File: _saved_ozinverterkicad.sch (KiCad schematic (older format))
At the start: 83 parts, among them P1 CONN_02X05, P2 status, P3 on/off, P4 temp, P5 ct sense, P6 Active mains, P7 neutral mains, P8 systemled, Q2 tip35c, T1 12vac transforme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

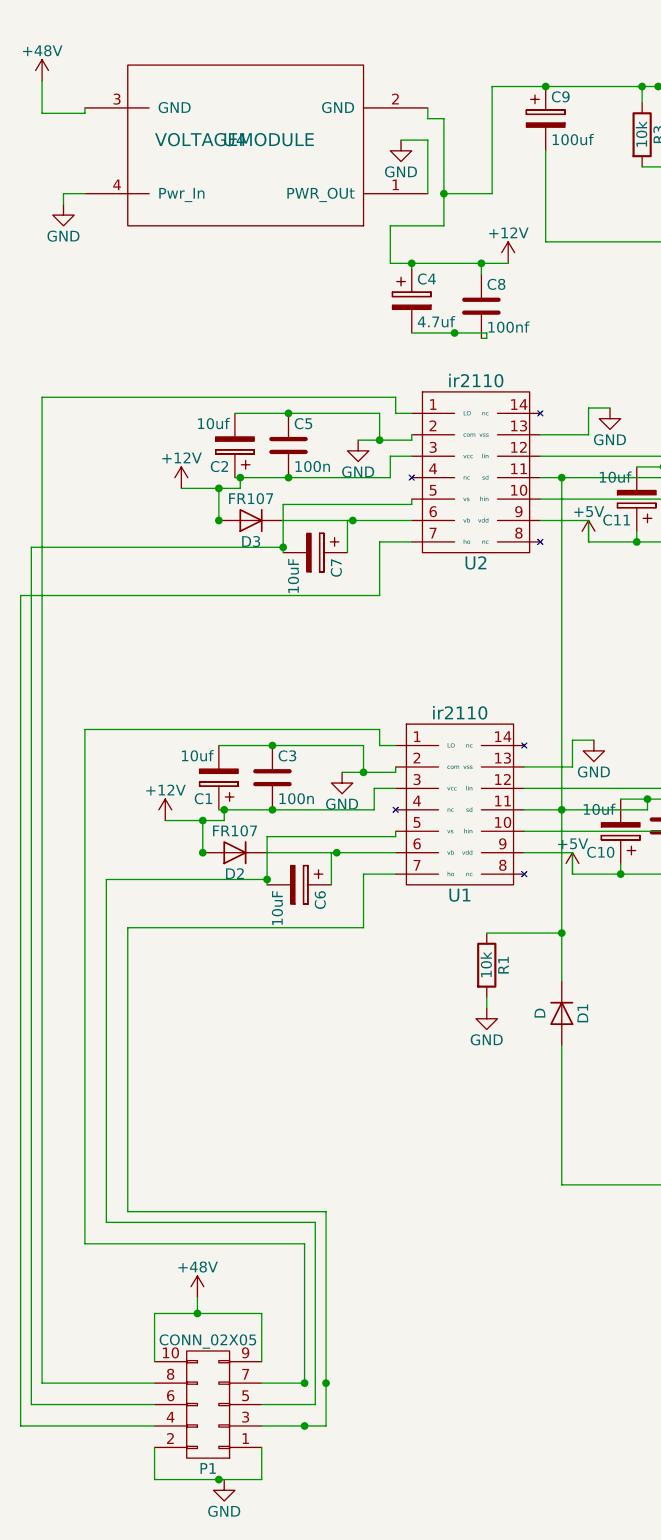
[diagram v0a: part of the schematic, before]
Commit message: changed plug around for correct pinout
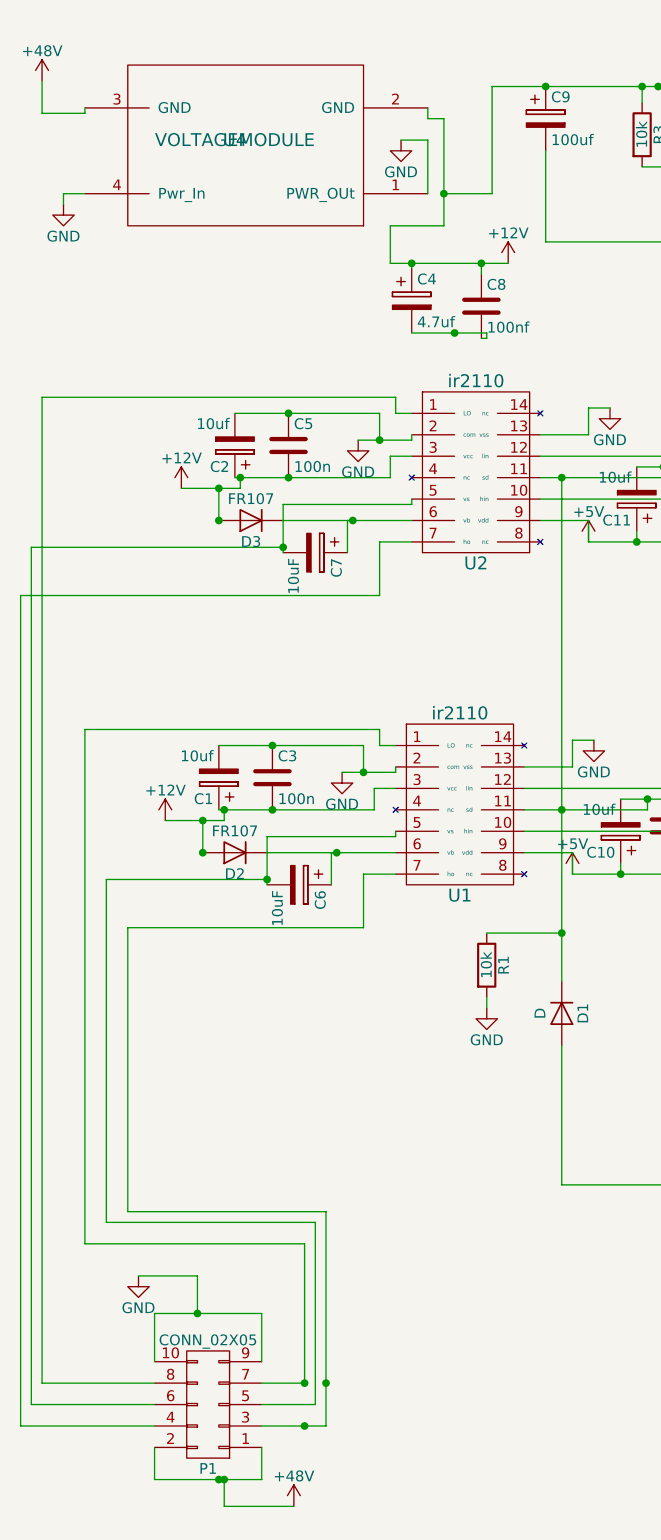
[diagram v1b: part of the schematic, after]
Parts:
- RV1, RV2: footprint Discret:RV2X4 -> Potentiometers:Potentiometer_Trimmer_ACP_CA9v_Horizontal_Px10.0mm_Py5.0mm
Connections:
- net +48V: now also P1.1 (P1), P1.2 (P2); no longer P1.10 (P10), P1.9 (P9)
- net GND: now also P1.10 (P10), P1.9 (P9); no longer P1.1 (P1), P1.2 (P2)
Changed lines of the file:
@@
 F 0 "RV1" H 7000 2695 50  0000 C CNN
 F 1 "2k" H 7000 2775 50  0000 C CNN
-F 2 "Discret:RV2X4" H 7000 2775 50  0001 C CNN
+F 2 "Potentiometers:Potentiometer_Trimmer_ACP_CA9v_Horizontal_Px10.0mm_Py5.0mm" H 7000 2775 50  0001 C CNN
 F 3 "" H 7000 2775 50  0000 C CNN
 	1    7000 2775
@@
 L GND #PWR019
 U 1 1 57CB3A5E
-P 1500 7400
-F 0 "#PWR019" H 1500 7150 50  0001 C CNN
-F 1 "GND" H 1500 7250 50  0000 C CNN
-F 2 "" H 1500 7400 50  0000 C CNN
-F 3 "" H 1500 7400 50  0000 C CNN
-	1    1500 7400
+P 1100 6450
+F 0 "#PWR019" H 1100 6200 50  0001 C CNN
+F 1 "GND" H 1100 6300 50  0000 C CNN
+F 2 "" H 1100 6450 50  0000 C CNN
+F 3 "" H 1100 6450 50  0000 C CNN
+	1    1100 6450
 	1    0    0    -1
 $EndComp
@@
 L +48V #PWR020
 U 1 1 57CB3D96
-P 1375 6550
-F 0 "#PWR020" H 1375 6400 50  0001 C CNN
-F 1 "+48V" H 1375 6690 50  0000 C CNN
-F 2 "" H 1375 6550 50  0000 C CNN
-F 3 "" H 1375 6550 50  0000 C CNN
-	1    1375 6550
+P 1825 7525
+F 0 "#PWR020" H 1825 7375 50  0001 C CNN
+F 1 "+48V" H 1825 7665 50  0000 C CNN
+F 2 "" H 1825 7525 50  0000 C CNN
+F 3 "" H 1825 7525 50  0000 C CNN
+	1    1825 7525
 	1    0    0    -1
 $EndComp
@@
 	1675 6625 1675 6850
 Wire Wire Line
-	1375 6550 1375 6625
+	1375 6450 1375 6625
 Connection ~ 1375 6625
 Wire Wire Line
@@
 	2275 1725 2275 1550
 Wire Wire Line
-	2525 1550 2275 1550
-Wire Wire Line
-	2525 1050 2525 1550
+	2275 1550 2525 1550
+Wire Wire Line
+	2525 1550 2525 1050
 Connection ~ 2525 1400
 Wire Wire Line
@@
 F 0 "RV2" H 8750 1245 50  0000 C CNN
 F 1 "2k" H 8750 1325 50  0000 C CNN
-F 2 "Discret:RV2X4" H 8750 1325 50  0001 C CNN
+F 2 "Potentiometers:Potentiometer_Trimmer_ACP_CA9v_Horizontal_Px10.0mm_Py5.0mm" H 8750 1325 50  0001 C CNN
 F 3 "" H 8750 1325 50  0000 C CNN
 	1    8750 1325
@@
 	2450 1150 2325 1150
 Wire Wire Line
-	2450 1050 2525 1050
+	2525 1050 2450 1050
+Wire Wire Line
+	1100 6450 1375 6450
+Wire Wire Line
+	1500 7400 1500 7525
+Wire Wire Line
+	1500 7525 1825 7525
+Connection ~ 1500 7400
 $EndSCHEMATC
